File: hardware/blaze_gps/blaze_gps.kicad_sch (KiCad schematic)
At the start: 34 parts, among them J1 JTAG, SW1 SW_SPST, SW2 SW_SPDT, SW3 SW_SPST, U1 ZED-F9R, U2 TCAN1044VDDFR, U3 STM32H503KBUx

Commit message: Added capacitors, connected gps uart
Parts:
- added C14: 1.0uF, symbol Device:C
- added C15: 2.2uF, symbol Device:C
- added C16: 0.1uF, symbol Device:C
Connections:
- net +3V3: now also C14.1, C16.1
- net DIRECTION: now also U3.13 (PA7); no longer U3.10 (PA4)
- net GND: now also C14.2, C15.2, C16.2
- net GOFENCE_STAT: now also U3.10 (PA4); no longer U3.7 (PA1)
- net GPS_RX: now also U3.7 (PA1)
- net GPS_TX: now also U3.8 (PA2)
- net RTK_STAT: now also U3.9 (PA3); no longer U3.6 (PA0)
- net TX_READY: now also U3.11 (PA5); no longer U3.8 (PA2)
- net VBATT_GPS: now also C15.1
- net WHEEL_TICKS: now also U3.12 (PA6); no longer U3.9 (PA3)
- no-connect marks 27 -> 25

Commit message: Filled in title block for GPS
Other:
- company: (none) -> UCSC Rocket Team
- title: (none) -> Blaze GPS
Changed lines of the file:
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@@
 	(generator_version "8.0")
 	(paper "A4")
+	(title_block
+		(title "Blaze GPS")
+		(date "2024-09-23")
+		(rev "1")
+		(company "UCSC Rocket Team")
+		(comment 1 "Designed by Julian Barbera")
+	)

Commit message: Removed audio, neopixel, can2 from interconnect
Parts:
- added J2: Conn_01x30, symbol Connector_Generic:Conn_01x30
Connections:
- net +3V3: now also J2.12 (Pin_12), J2.18 (Pin_18), J2.29 (Pin_29), J2.30 (Pin_30)
- net +5V: now also J2.11 (Pin_11), J2.27 (Pin_27), J2.28 (Pin_28)
- net CANH: now also J2.24 (Pin_24)
- net CANL: now also J2.23 (Pin_23)
- net GND: now also J2.14 (Pin_14), J2.15 (Pin_15), J2.21 (Pin_21), J2.22 (Pin_22), J2.3 (Pin_3), J2.4 (Pin_4)
- net PPS: now also J2.13 (Pin_13)
- new net VBATT: J2.1 (Pin_1), J2.2 (Pin_2)
- no-connect marks 25 -> 37

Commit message: GPS Footprint Assingments
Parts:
- C1, C10, C11, C12, C13, C14, C15, C16, C2, C3, C4, C5, C6, C7, C8, C9: footprint (none) -> Capacitor_SMD:C_0603_1608Metric
- D1, D5: footprint (none) -> Diode_SMD:D_0603_1608Metric
- J1: footprint (none) -> Connector_PinHeader_1.00mm:PinHeader_2x05_P1.00mm_Vertical_SMD
- J2: footprint (none) -> DF17:HRS_DF17_1.0H_-30DP-0.5V_57_
- R1, R2, R3, R4, R5: footprint (none) -> Resistor_SMD:R_0603_1608Metric
- SW1, SW3: footprint (none) -> Button_Switch_SMD:SW_SPST_B3U-1000P
- SW2: footprint (none) -> Button_Switch_SMD:Nidec_Copal_CAS-120A
- U2: footprint (none) -> Package_SON:Texas_VSON-HR-8_1.5x2mm_P0.5mm

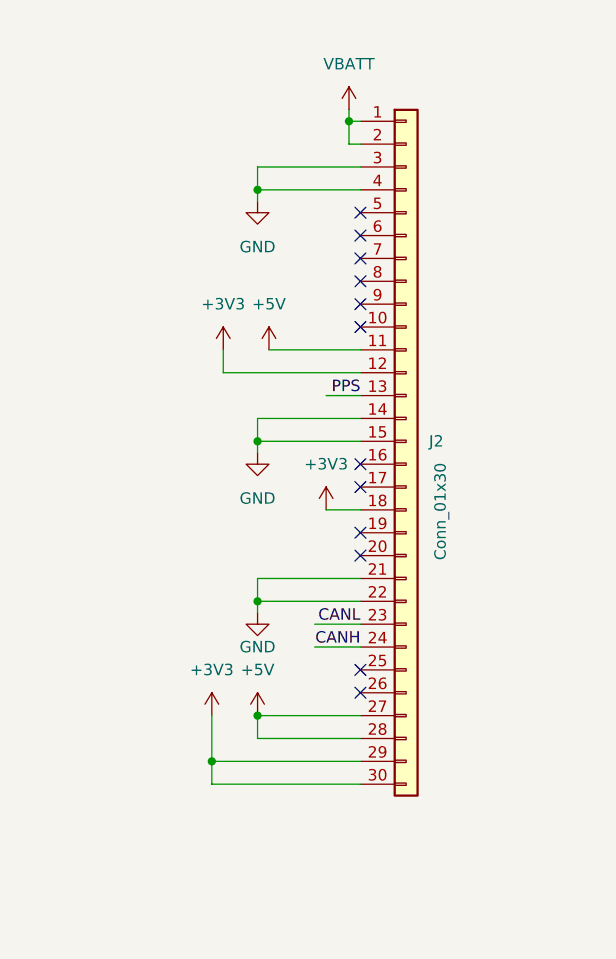
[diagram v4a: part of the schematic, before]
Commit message: Added mirror interconnect and PCB to gps
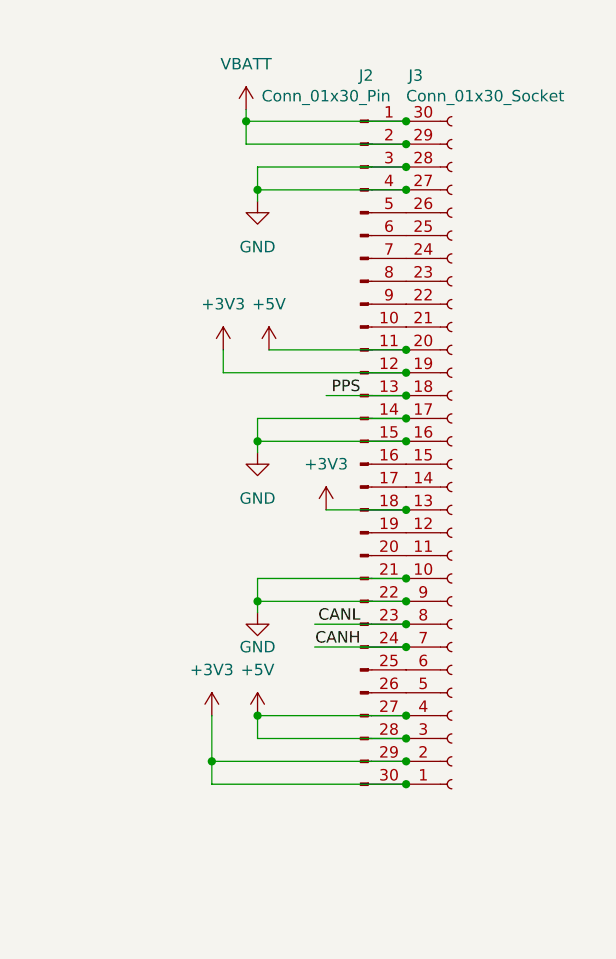
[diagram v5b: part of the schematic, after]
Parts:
- removed J2: Conn_01x30, DF17:HRS_DF17_1.0H_-30DP-0.5V_57_, symbol Connector_Generic:Conn_01x30
- added J2: Conn_01x30_Pin, Blaze_Library:HRS_DF17_1.0H_-30DP-0.5V_57_, symbol Connector:Conn_01x30_Pin
- added J3: Conn_01x30_Socket, Blaze_Library:HRS_DF17_1.0H_-30DP-0.5V_57_, symbol Connector:Conn_01x30_Socket
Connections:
- net +3V3: now also J2.12 (Pin_12), J2.18 (Pin_18), J2.29 (Pin_29), J2.30 (Pin_30), J3.1 (Pin_1), J3.13 (Pin_13), J3.19 (Pin_19), J3.2 (Pin_2)
- net +5V: now also J2.11 (Pin_11), J2.27 (Pin_27), J2.28 (Pin_28), J3.20 (Pin_20), J3.3 (Pin_3), J3.4 (Pin_4)
- net CANH: now also J2.24 (Pin_24), J3.7 (Pin_7)
- net CANL: now also J2.23 (Pin_23), J3.8 (Pin_8)
- net GND: now also J2.14 (Pin_14), J2.15 (Pin_15), J2.21 (Pin_21), J2.22 (Pin_22), J2.3 (Pin_3), J2.4 (Pin_4), J3.10 (Pin_10), J3.16 (Pin_16), J3.17 (Pin_17), J3.27 (Pin_27), J3.28 (Pin_28), J3.9 (Pin_9)
- net PPS: now also J2.13 (Pin_13), J3.18 (Pin_18)
- net VBATT: now also J2.1 (Pin_1), J2.2 (Pin_2), J3.29 (Pin_29), J3.30 (Pin_30)
- new net: J2.10 (Pin_10), J3.21 (Pin_21)
- new net: J2.16 (Pin_16), J3.15 (Pin_15)
- new net: J2.17 (Pin_17), J3.14 (Pin_14)
- new net: J2.19 (Pin_19), J3.12 (Pin_12)
- new net: J2.20 (Pin_20), J3.11 (Pin_11)
- new net: J2.25 (Pin_25), J3.6 (Pin_6)
- new net: J2.26 (Pin_26), J3.5 (Pin_5)
- new net: J2.5 (Pin_5), J3.26 (Pin_26)
- new net: J2.6 (Pin_6), J3.25 (Pin_25)
- new net: J2.7 (Pin_7), J3.24 (Pin_24)
- new net: J2.8 (Pin_8), J3.23 (Pin_23)
- new net: J2.9 (Pin_9), J3.22 (Pin_22)
- no-connect marks 37 -> 25
